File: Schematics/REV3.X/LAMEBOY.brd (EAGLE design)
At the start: 45.7 x 67.3 mm, 65 parts, among them IC1 PCF8574T, IC3 MCP73831, Q1 12MHz, U1 USD-SOCKETMICROSDEBAY

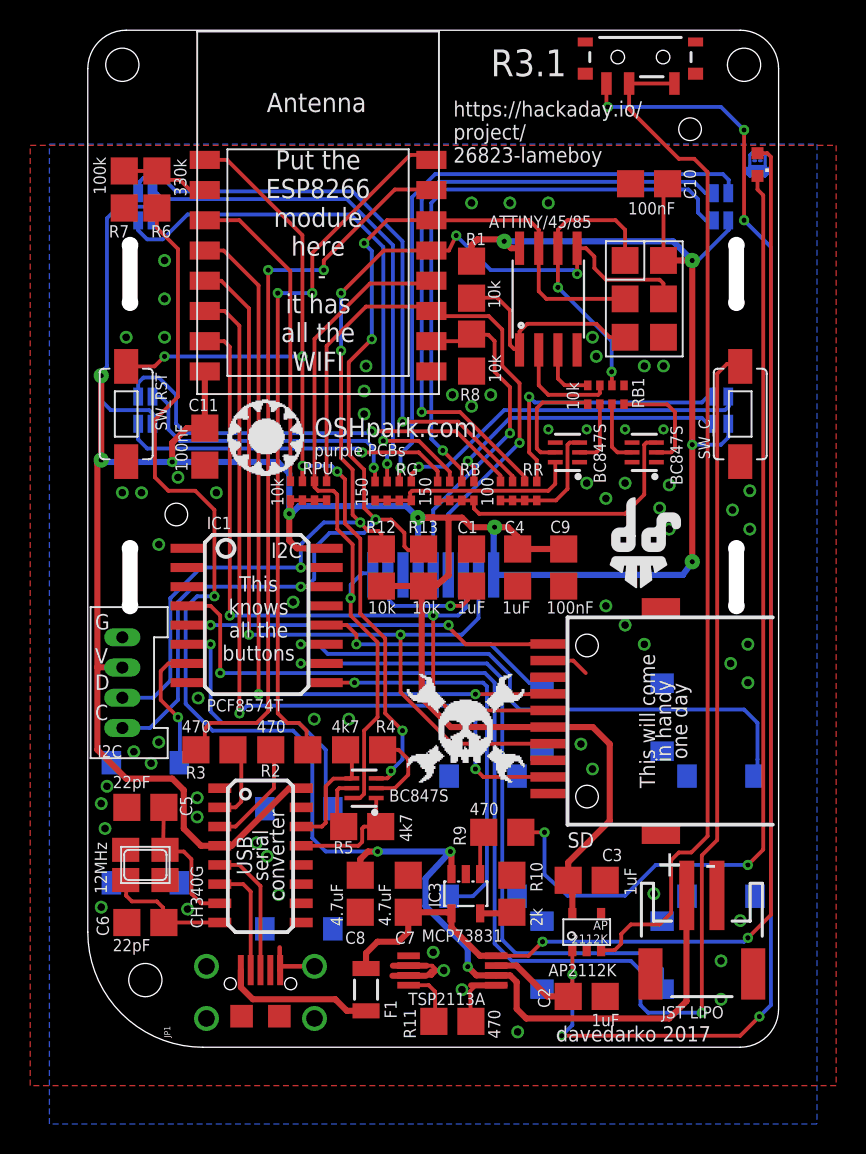
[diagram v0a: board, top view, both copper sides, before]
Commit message: moved 3.1 to 3.X
added pull down power switch
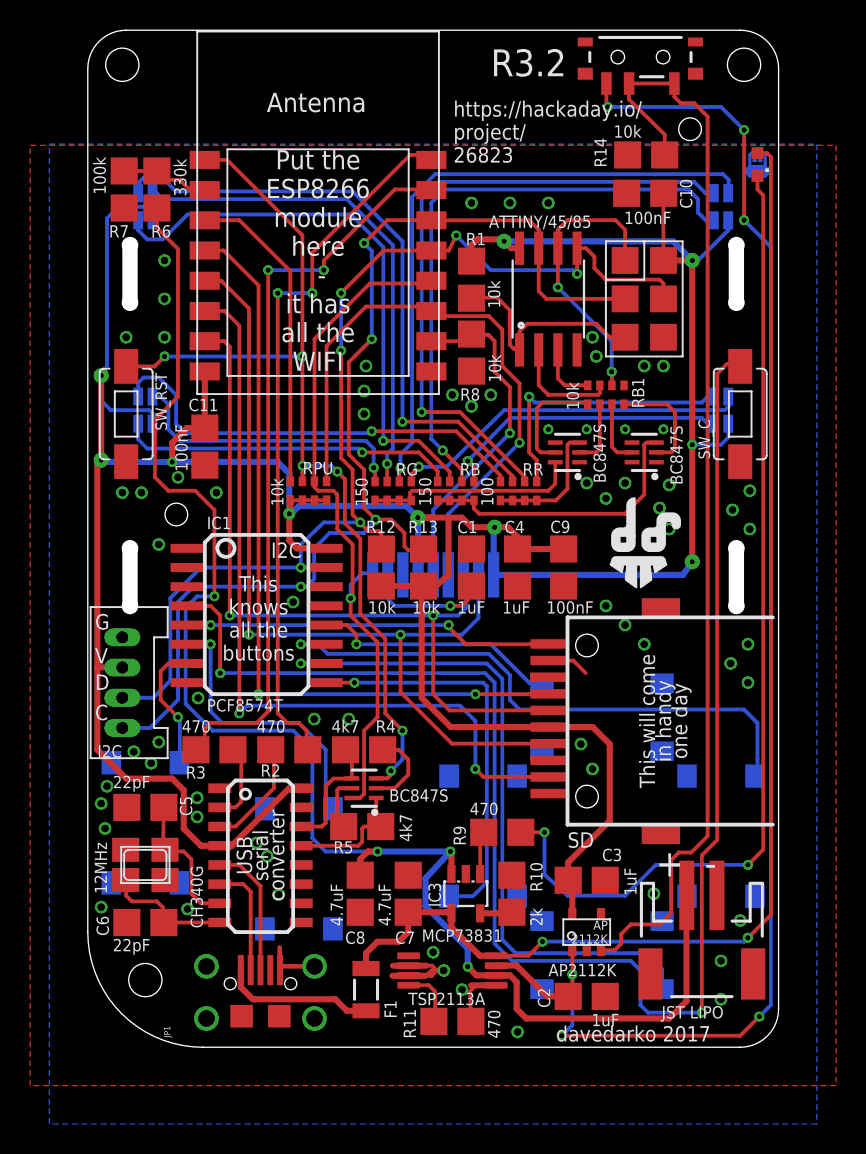
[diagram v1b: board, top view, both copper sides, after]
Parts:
- removed U$12: (no value), LOGOS:HACKADAY_LOGO
- removed U$5: (no value), LOGOS:OSHPARK_LOGO
- added R14: 10k, rcl:ONEFITSALL
- moved C10 0.68 mm to (36.9, 56.5)
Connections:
- net GND: now also R14.P$2
- net VREG_EN: now also R14.P$1
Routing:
- net VREG_EN: track 68.2 -> 72.6 mm
- net VCC: track 234.1 -> 234.9 mm
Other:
- board text added: "R3.2"
- board text added: "https://hackaday.io/ project/ 26823"
- board text removed: "R3.1"
- board text removed: "https://hackaday.io/ project/ 26823-lameboy"
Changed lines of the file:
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@@
 <text x="24.1935" y="58.547" size="1.016" layer="25" ratio="12">https://hackaday.io/
 project/
-26823-lameboy</text>
+26823</text>
 <text x="30.988" y="0.381" size="1.016" layer="25" ratio="12">davedarko 2017</text>
 <wire x1="9.779" y1="17.653" x2="9.271" y2="17.145" width="0.254" layer="25"/>
@@
 <text x="45.339" y="55.88" size="0.8128" layer="26" ratio="12" rot="MR0">USB</text>
 <text x="30.48" y="4.699" size="0.8128" layer="25" ratio="12">AP2112K</text>
-<text x="26.67" y="64.262" size="1.778" layer="25" ratio="12">R3.1</text>
+<text x="26.67" y="64.262" size="1.778" layer="25" ratio="12">R3.2</text>
 </plain>
 <attributes>
@@
 <attribute name="VALUE" x="30.353" y="28.702" size="0.8128" layer="25" ratio="12"/>
 </element>
-<element name="C10" library="rcl" package="ONEFITSALL" value="100nF" x="37.1475" y="57.15" smashed="yes">
-<attribute name="NAME" x="40.259" y="56.134" size="0.8128" layer="25" ratio="12" rot="R90"/>
-<attribute name="VALUE" x="35.7505" y="55.118" size="0.8128" layer="25" ratio="12"/>
+<element name="C10" library="rcl" package="ONEFITSALL" value="100nF" x="36.8935" y="56.515" smashed="yes">
+<attribute name="NAME" x="40.005" y="55.499" size="0.8128" layer="25" ratio="12" rot="R90"/>
+<attribute name="VALUE" x="35.4965" y="54.483" size="0.8128" layer="25" ratio="12"/>
 </element>
 <element name="C11" library="rcl" package="ONEFITSALL" value="100nF" x="7.747" y="39.751" smashed="yes" rot="R90">
@@
 <attribute name="VALUE" x="6.604" y="38.1" size="0.8128" layer="25" ratio="12" rot="R90"/>
 </element>
-<element name="U$5" library="LOGOS" package="OSHPARK_LOGO" value="" x="20.701" y="40.386"/>
 <element name="U$11" library="LOGOS" package="DAVEDARKO2_LOGO" value="" x="36.449" y="32.639"/>
-<element name="U$12" library="LOGOS" package="HACKADAY_LOGO" value="" x="24.9555" y="20.7645"/>
 <element name="U$13" library="LOGOS" package="DAVEDARKO_GOLD" value="" x="34.036" y="12.827" rot="MR0"/>
 <element name="JP1" library="SparkFun-Connectors" package="USB-AB-MICRO-SMD_SLOT" value="USB_MICROB_PLUG-IDK" x="11.43" y="1.905" rot="R90"/>
+<element name="R14" library="rcl" package="ONEFITSALL" value="10k" x="36.957" y="59.055" smashed="yes" rot="R180">
+<attribute name="NAME" x="33.528" y="60.198" size="0.8128" layer="25" ratio="12" rot="R270"/>
+<attribute name="VALUE" x="34.798" y="60.198" size="0.8128" layer="25" ratio="12"/>
+</element>
 </elements>
 <signals>
@@
 <wire x1="12.73" y1="5.355" x2="12.73" y2="5.08" width="0.3048" layer="1"/>
 <wire x1="12.73" y1="5.08" x2="12.7" y2="5.08" width="0.3048" layer="1"/>
+<contactref element="R14" pad="P$2"/>
 </signal>
 <signal name="VCC">
@@
 <contactref element="C11" pad="P$2"/>
 <wire x1="38.1" y1="52.07" x2="38.1" y2="57.1475" width="0.254" layer="1"/>
-<wire x1="38.1" y1="57.1475" x2="38.3725" y2="57.15" width="0.254" layer="1"/>
-<wire x1="38.1" y1="57.1525" x2="38.3725" y2="57.15" width="0.254" layer="1"/>
+<wire x1="38.1" y1="57.1475" x2="38.1185" y2="56.515" width="0.254" layer="1"/>
+<wire x1="38.1" y1="57.1525" x2="38.1185" y2="56.515" width="0.254" layer="1"/>
 <wire x1="27.527" y1="53.372" x2="27.559" y2="53.34" width="0.4064" layer="1"/>
 <wire x1="31.496" y1="32.975" x2="28.448" y2="32.975" width="0.4064" layer="1"/>
@@
 <wire x1="39.116" y1="12.8905" x2="39.9415" y2="12.8905" width="0.254" layer="1"/>
 <wire x1="39.9415" y1="12.8905" x2="41.021" y2="13.97" width="0.254" layer="1"/>
-<wire x1="41.021" y1="13.97" x2="41.021" y2="57.912" width="0.254" layer="1"/>
-<wire x1="41.021" y1="57.912" x2="40.132" y2="58.801" width="0.254" layer="1"/>
-<wire x1="40.132" y1="58.801" x2="39.116" y2="58.801" width="0.254" layer="1"/>
-<wire x1="39.116" y1="58.801" x2="35.826" y2="62.091" width="0.254" layer="1"/>
-<wire x1="35.826" y1="62.091" x2="35.826" y2="63.782" width="0.254" layer="1"/>
+<wire x1="41.021" y1="13.97" x2="41.021" y2="61.595" width="0.254" layer="1"/>
+<wire x1="41.021" y1="61.595" x2="40.132" y2="62.484" width="0.254" layer="1"/>
 <wire x1="33.97" y1="6.42" x2="34.868" y2="6.42" width="0.254" layer="1"/>
 <wire x1="34.868" y1="6.42" x2="35.306" y2="6.858" width="0.254" layer="1"/>
@@
 <wire x1="37.846" y1="8.128" x2="38.608" y2="8.89" width="0.254" layer="1"/>
 <wire x1="38.608" y1="8.89" x2="38.608" y2="12.3825" width="0.254" layer="1"/>
+<contactref element="R14" pad="P$1"/>
+<wire x1="40.132" y1="62.484" x2="39.243" y2="62.484" width="0.254" layer="1"/>
+<wire x1="39.243" y1="62.484" x2="38.826" y2="62.901" width="0.254" layer="1"/>
+<wire x1="38.826" y1="63.782" x2="38.826" y2="62.901" width="0.254" layer="1"/>
+<wire x1="38.182" y1="59.055" x2="38.182" y2="60.407" width="0.254" layer="1"/>
+<wire x1="38.182" y1="60.407" x2="35.814" y2="62.738" width="0.254" layer="1"/>
+<wire x1="35.814" y1="62.738" x2="35.814" y2="63.77" width="0.254" layer="1"/>
+<wire x1="35.814" y1="63.77" x2="35.826" y2="63.782" width="0.254" layer="1"/>
 </signal>
 <signal name="N$11">

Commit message: minor changes to rev3.1
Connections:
- net GPIO0 renamed GPIO0/LCD_RST
- net GPIO15 renamed GPIO15/LCD_CS
- net GPIO2 renamed GPIO2/LCD_DC
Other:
- board text added: "R3.2.1"
- board text removed: "R3.2"
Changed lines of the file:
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@@
 <layer number="25" name="tNames" color="7" fill="1" visible="yes" active="yes"/>
 <layer number="26" name="bNames" color="7" fill="1" visible="yes" active="yes"/>
-<layer number="27" name="tValues" color="7" fill="1" visible="yes" active="yes"/>
-<layer number="28" name="bValues" color="7" fill="1" visible="yes" active="yes"/>
+<layer number="27" name="tValues" color="7" fill="1" visible="no" active="yes"/>
+<layer number="28" name="bValues" color="7" fill="1" visible="no" active="yes"/>
 <layer number="29" name="tStop" color="7" fill="3" visible="no" active="yes"/>
 <layer number="30" name="bStop" color="7" fill="6" visible="no" active="yes"/>
@@
 <text x="45.339" y="55.88" size="0.8128" layer="26" ratio="12" rot="MR0">USB</text>
 <text x="30.48" y="4.699" size="0.8128" layer="25" ratio="12">AP2112K</text>
-<text x="26.67" y="64.262" size="1.778" layer="25" ratio="12">R3.2</text>
+<text x="26.67" y="64.262" size="1.27" layer="25" ratio="12">R3.2.1</text>
+<circle x="22.86" y="6.223" radius="0.40160625" width="0.4064" layer="25"/>
+<wire x1="1.524" y1="57.15" x2="1.524" y2="56.515" width="0.1524" layer="25"/>
+<wire x1="3.302" y1="57.15" x2="3.302" y2="56.515" width="0.1524" layer="25"/>
+<wire x1="3.683" y1="57.15" x2="3.683" y2="56.515" width="0.1524" layer="25"/>
+<wire x1="5.461" y1="57.15" x2="5.461" y2="56.515" width="0.1524" layer="25"/>
+<wire x1="3.81" y1="40.64" x2="3.81" y2="41.148" width="0.1524" layer="26"/>
+<wire x1="3.81" y1="54.61" x2="3.81" y2="54.102" width="0.1524" layer="26"/>
+<wire x1="41.91" y1="54.102" x2="41.91" y2="54.864" width="0.1524" layer="26"/>
+<wire x1="41.91" y1="40.64" x2="41.91" y2="41.402" width="0.1524" layer="26"/>
 </plain>
 <attributes>
@@
 <wire x1="22.38375" y1="4.73075" x2="22.76475" y2="4.73075" width="0.254" layer="1"/>
 <wire x1="22.76475" y1="4.73075" x2="23.114" y2="5.08" width="0.254" layer="1"/>
-<via x="22.86" y="6.2865" extent="1-16" drill="0.5"/>
-<via x="23.5585" y="5.08" extent="1-16" drill="0.5"/>
+<via x="24.003" y="6.096" extent="1-16" drill="0.5"/>
+<via x="23.3045" y="4.826" extent="1-16" drill="0.5"/>
 <via x="28.448" y="1.016" extent="1-16" drill="0.5"/>
 <via x="24.765" y="3.81" extent="1-16" drill="0.5"/>
@@
 <wire x1="26.179" y1="17.89" x2="25.654" y2="18.415" width="0.254" layer="1"/>
 </signal>
-<signal name="GPIO15">
+<signal name="GPIO15/LCD_CS">
 <contactref element="X1" pad="10"/>
 <contactref element="R8" pad="P$1"/>
@@
 <wire x1="17.478" y1="19.32" x2="17.063" y2="19.685" width="0.254" layer="1"/>
 </signal>
-<signal name="GPIO0">
+<signal name="GPIO0/LCD_RST">
 <contactref element="U$3" pad="6"/>
 <contactref element="X1" pad="12"/>
@@
 <wire x1="8.129" y1="54.737" x2="7.74" y2="54.729" width="0.254" layer="1"/>
 </signal>
-<signal name="GPIO2">
+<signal name="GPIO2/LCD_DC">
 <contactref element="RPU" pad="5"/>
 <contactref element="X1" pad="11"/>
